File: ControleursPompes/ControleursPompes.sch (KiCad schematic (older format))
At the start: 64 parts, among them J1 SWD, J18 Alim 5V, J19 TOR, J2 PWR_IN, J3 I2C 5V, J4 I2C 3.3V, J5 ARIG Interf, Q1 BSS138, Q2 BSS138, SW1 Reset, SW2 Reset, SW3 Reset, U1 AMS1117-3.3, U2 STM32F103C8Tx, Y1 16Mhz

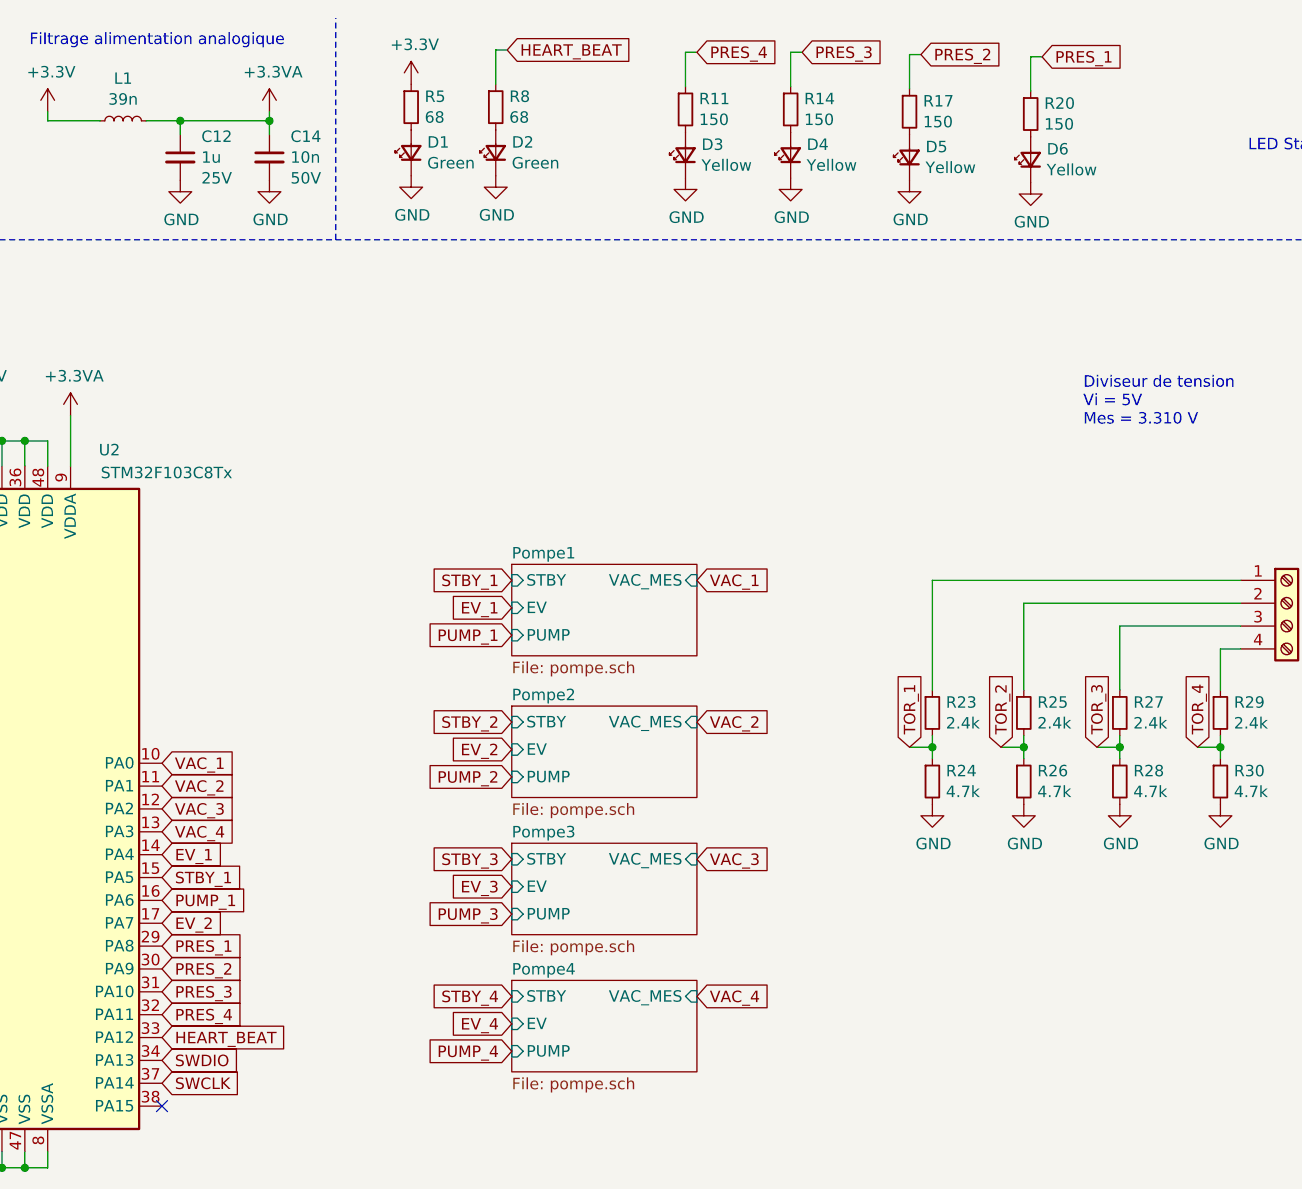
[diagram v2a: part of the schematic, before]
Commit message: Erreur entre la sérigraphie et l'assignation des PIN
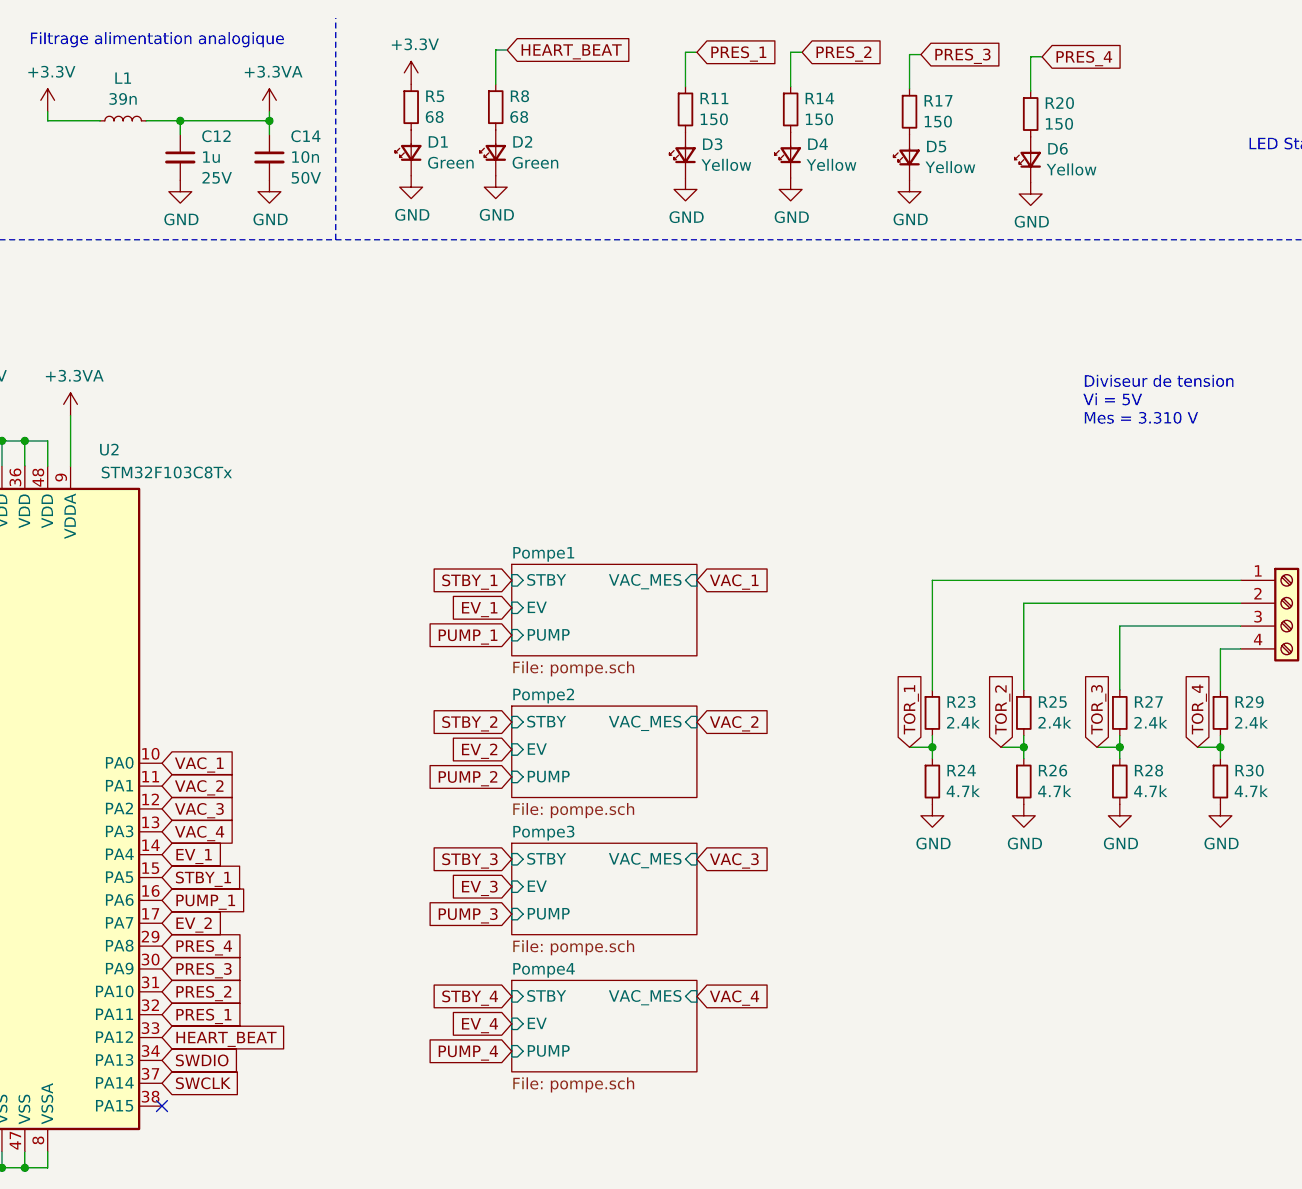
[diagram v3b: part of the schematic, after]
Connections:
- net PRES_1: now also R11.1, U2.32 (PA11); no longer R20.1, U2.29 (PA8)
- net PRES_2: now also R14.1, U2.31 (PA10); no longer R17.1, U2.30 (PA9)
- net PRES_3: now also R17.1, U2.30 (PA9); no longer R14.1, U2.31 (PA10)
- net PRES_4: now also R20.1, U2.29 (PA8); no longer R11.1, U2.32 (PA11)
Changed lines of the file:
@@
 Text GLabel 2260 1670 2    50   Input ~ 0
 SCL_33
+Text GLabel 5810 4840 2    50   Input ~ 0
+PRES_1
+Text GLabel 5810 4740 2    50   Input ~ 0
+PRES_2
+Text GLabel 5810 4640 2    50   Input ~ 0
+PRES_3
 Text GLabel 5810 4540 2    50   Input ~ 0
+PRES_4
+Text GLabel 8150 630  2    50   Input ~ 0
 PRES_1
-Text GLabel 5810 4640 2    50   Input ~ 0
+Text GLabel 8610 630  2    50   Input ~ 0
 PRES_2
-Text GLabel 5810 4740 2    50   Input ~ 0
+Text GLabel 9130 640  2    50   Input ~ 0
 PRES_3
-Text GLabel 5810 4840 2    50   Input ~ 0
-PRES_4
 Text GLabel 9660 650  2    50   Input ~ 0
-PRES_1
-Text GLabel 9130 640  2    50   Input ~ 0
-PRES_2
-Text GLabel 8610 630  2    50   Input ~ 0
-PRES_3
-Text GLabel 8150 630  2    50   Input ~ 0
 PRES_4
 $Comp
